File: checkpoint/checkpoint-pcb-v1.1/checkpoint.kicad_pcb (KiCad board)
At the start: 4 copper layers, 85.2 x 39.6 mm, 113 parts, among them J1 T0, J10 CAN_OUT, J11 BOOT, J12 Y_ENDSTOP, J13 I2C, J14 SERVO, J15 RGB, J16 SWD, J17 USB_C_Receptacle_USB2.0_16P, J18 PWR_OUT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

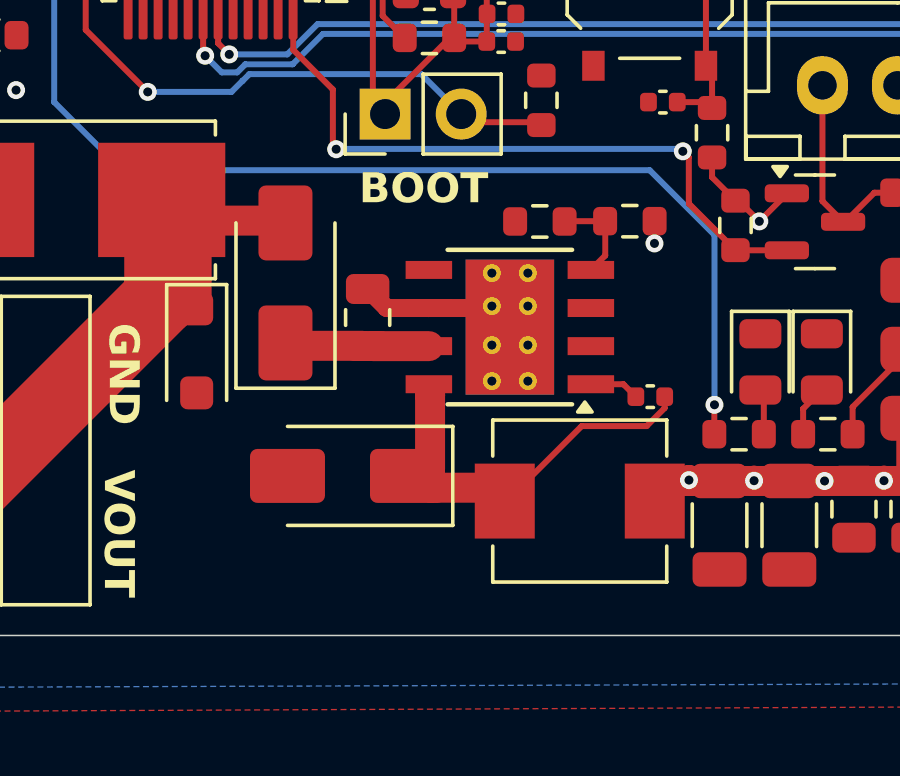
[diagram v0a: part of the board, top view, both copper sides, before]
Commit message: feat: add inductor to support 3A@5V output
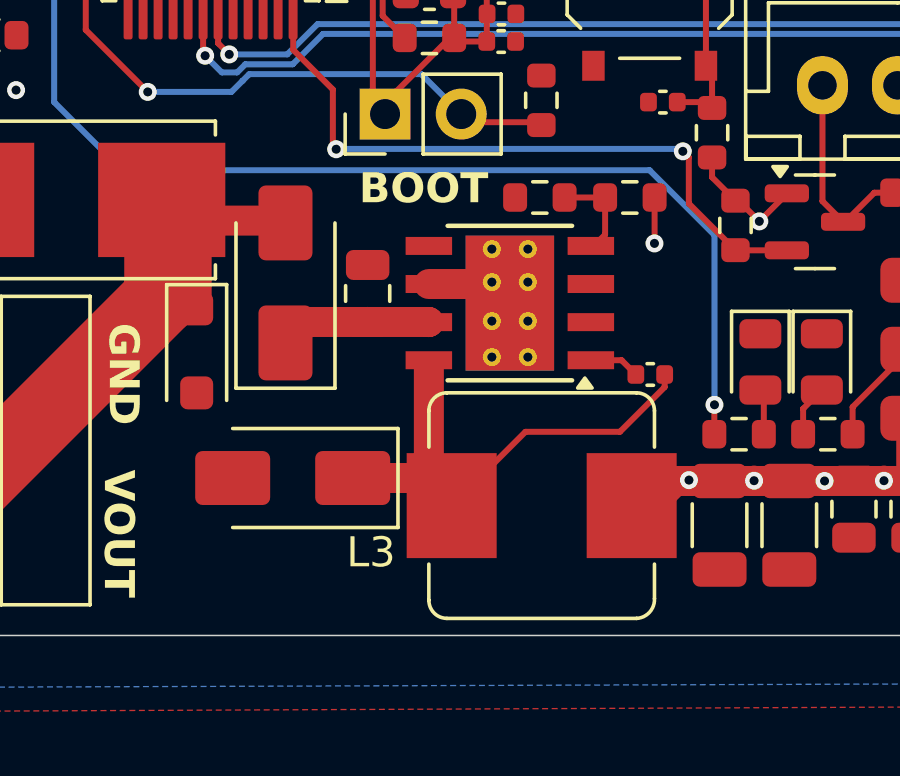
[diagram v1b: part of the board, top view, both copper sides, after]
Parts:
- L3: value 22uH -> 47uH; footprint Library:SMMS0530 -> Library:L_Bourns_SRP7050WA_7.9x7.3mm
- moved D11 1.83 mm to (65.2, 68.5)
- moved L3 1.28 mm to (73.5, 69.4)
- moved C27 0.80 mm to (67.7, 62.3)
- moved U6 0.80 mm to (72.5, 62.6)
- moved R36 0.80 mm to (73.5, 59.1)
- moved R35 0.79 mm to (76.5, 59.1)
- moved C28 0.74 mm to (77.1, 65.0)
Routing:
- net Net-(D11-K): track 11.9 -> 18.1 mm
- net GND: track 32.1 -> 29.4 mm
- net Net-(D10-K): track 4.19 -> 5.07 mm
- net +5V: track 16.2 -> 16.8 mm

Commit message: chore: update component rotation
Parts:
- C1, C10, C14, C18, C19, C2, C21, C22, C24, C26, C28, C3, C4, C5, C6, C7, C9: value 0.1uF -> 100nF
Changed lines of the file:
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@@
 		(sheetname "Thermistors")
 		(sheetfile "thermistors.kicad_sch")
-		(attr through_hole exclude_from_pos_files exclude_from_bom)
+		(attr through_hole exclude_from_pos_files)
 		(fp_line
 			(start -1.6 -2.75)
@@
 			)
 		)
-		(property "Value" "0.1uF"
+		(property "Value" "100nF"
 			(at 0 1.16 180)
 			(layer "F.Fab")
@@
 			)
 		)
-		(property "Value" "0.1uF"
+		(property "Value" "100nF"
 			(at 0 1.16 180)
 			(layer "F.Fab")
@@
 			)
 		)
-		(property "Value" "0.1uF"
+		(property "Value" "100nF"
 			(at 0.35 1.42 180)
 			(layer "F.Fab")
@@
 		(sheetname "CANBUS")
 		(sheetfile "canbus.kicad_sch")
-		(attr through_hole exclude_from_pos_files exclude_from_bom)
+		(attr through_hole exclude_from_pos_files)
 		(fp_line
 			(start -1.33 3.87)
@@
 			)
 		)
-		(property "Value" "0.1uF"
+		(property "Value" "100nF"
 			(at -0.75 0.1225 90)
 			(layer "F.Fab")
@@
 			)
 		)
-		(property "Value" "0.1uF"
+		(property "Value" "100nF"
 			(at 0 1.16 180)
 			(layer "F.Fab")
@@
 			)
 		)
-		(property "Value" "0.1uF"
+		(property "Value" "100nF"
 			(at 1.905589 1.16 90)
 			(layer "F.Fab")
@@
 			)
 		)
-		(property "Value" "0.1uF"
+		(property "Value" "100nF"
 			(at 0.0025 1.14 0)
 			(layer "F.Fab")
@@
 		(sheetname "Thermistors")
 		(sheetfile "thermistors.kicad_sch")
-		(attr through_hole exclude_from_pos_files exclude_from_bom)
+		(attr through_hole exclude_from_pos_files)
 		(fp_line
 			(start -1.6 -2.75)
@@
 		(sheetname "CANBUS")
 		(sheetfile "canbus.kicad_sch")
-		(attr through_hole exclude_from_pos_files exclude_from_bom)
+		(attr through_hole exclude_from_pos_files)
 		(fp_line
 			(start -2.56 3.51)
@@
 		(sheetname "Power")
 		(sheetfile "power.kicad_sch")
-		(attr through_hole exclude_from_pos_files exclude_from_bom)
+		(attr through_hole exclude_from_pos_files)
 		(fp_line
 			(start -2.84 4.9)
@@
 			)
 		)
-		(property "Value" "0.1uF"
+		(property "Value" "100nF"
 			(at 0.05 -1.05 180)
 			(layer "F.Fab")
@@
 		(sheetname "USB")
 		(sheetfile "usb.kicad_sch")
-		(attr through_hole exclude_from_pos_files exclude_from_bom)
+		(attr through_hole exclude_from_pos_files)
 		(fp_line
 			(start -1.33 3.87)
@@
 		(sheetname "Thermistors")
 		(sheetfile "thermistors.kicad_sch")
-		(attr through_hole exclude_from_pos_files exclude_from_bom)
+		(attr through_hole exclude_from_pos_files)
 		(fp_line
 			(start 1.33 1.27)
@@
 			)
 		)
-		(property "Value" "0.1uF"
+		(property "Value" "100nF"
 			(at -0.005 -0.98 0)
 			(layer "F.Fab")
@@
 		(sheetname "MCU")
 		(sheetfile "mcu.kicad_sch")
-		(attr through_hole exclude_from_pos_files exclude_from_bom)
+		(attr through_hole exclude_from_pos_files)
 		(fp_line
 			(start 7.56 3.51)
@@
 			)
 		)
-		(property "Value" "0.1uF"
+		(property "Value" "100nF"
 			(at 0.085 -1.05 90)
 			(layer "F.Fab")
@@
 			)
 		)
-		(property "Value" "0.1uF"
+		(property "Value" "100nF"
 			(at 0 1.16 0)
 			(layer "F.Fab")
@@
 		(sheetname "MCU")
 		(sheetfile "mcu.kicad_sch")
-		(attr through_hole exclude_from_pos_files exclude_from_bom)
+		(attr through_hole exclude_from_pos_files)
 		(fp_line
 			(start -1.33 -1.33)
@@
 		(sheetname "Thermistors")
 		(sheetfile "thermistors.kicad_sch")
-		(attr through_hole exclude_from_pos_files exclude_from_bom)
+		(attr through_hole exclude_from_pos_files)
 		(fp_line
 			(start -1.33 -1.33)
@@
 			)
 		)
-		(property "Value" "0.1uF"
+		(property "Value" "100nF"
 			(at 0 1.16 0)
 			(layer "F.Fab")
@@
 		(sheetname "Thermistors")
 		(sheetfile "thermistors.kicad_sch")
-		(attr through_hole exclude_from_pos_files exclude_from_bom)
+		(attr through_hole exclude_from_pos_files)
 		(fp_line
 			(start -1.6 -2.75)
@@
 		(sheetname "Thermistors")
 		(sheetfile "thermistors.kicad_sch")
-		(attr through_hole exclude_from_pos_files exclude_from_bom)
+		(attr through_hole exclude_from_pos_files)
 		(fp_line
 			(start -1.33 -1.33)
@@
 		(sheetname "Power")
 		(sheetfile "power.kicad_sch")
-		(attr smd exclude_from_pos_files exclude_from_bom)
+		(attr smd exclude_from_pos_files)
 		(fp_line
 			(start -3.76 -1.95)
@@
 			)
 		)
-		(property "Value" "0.1uF"
+		(property "Value" "100nF"
 			(at 0 0 0)
 			(layer "F.Fab")
@@
 		(sheetname "MCU")
 		(sheetfile "mcu.kicad_sch")
-		(attr through_hole exclude_from_pos_files exclude_from_bom)
+		(attr through_hole exclude_from_pos_files)
 		(fp_line
 			(start -1.33 -1.33)
@@
 			)
 		)
-		(property "Value" "0.1uF"
+		(property "Value" "100nF"
 			(at 0 1.025 90)
 			(layer "F.Fab")
@@
 			)
 		)
-		(property "Value" "0.1uF"
+		(property "Value" "100nF"
 			(at 0 1.14 0)
 			(layer "F.Fab")
@@
 		(sheetname "MCU")
 		(sheetfile "mcu.kicad_sch")
-		(attr through_hole exclude_from_pos_files exclude_from_bom)
+		(attr through_hole exclude_from_pos_files)
 		(fp_line
 			(start 7.56 3.51)
@@
 		(sheetname "Thermistors")
 		(sheetfile "thermistors.kicad_sch")
-		(attr through_hole exclude_from_pos_files exclude_from_bom)
+		(attr through_hole exclude_from_pos_files)
 		(fp_line
 			(start -1.6 -2.75)
@@
 			)
 		)
-		(property "Value" "0.1uF"
+		(property "Value" "100nF"
 			(at 0 1.16 90)
 			(layer "F.Fab")
@@
 		(sheetname "MCU")
 		(sheetfile "mcu.kicad_sch")
-		(attr through_hole exclude_from_pos_files exclude_from_bom)
+		(attr through_hole exclude_from_pos_files)
 		(fp_line
 			(start -1.6 -2.75)
@@
 			)
 		)
-		(property "Value" "0.1uF"
+		(property "Value" "100nF"
 			(at 0 1.16 180)
 			(layer "F.Fab")
@@
 		(sheetname "Thermistors")
 		(sheetfile "thermistors.kicad_sch")
-		(attr through_hole exclude_from_pos_files exclude_from_bom)
+		(attr through_hole exclude_from_pos_files)
 		(fp_line
 			(start 1.33 1.27)
@@
 		(sheetname "Thermistors")
 		(sheetfile "thermistors.kicad_sch")
-		(attr through_hole exclude_from_pos_files exclude_from_bom)
+		(attr through_hole exclude_from_pos_files)
 		(fp_line
 			(start -1.6 -2.75)
@@
 		(sheetname "Power")
 		(sheetfile "power.kicad_sch")
-		(attr through_hole exclude_from_pos_files exclude_from_bom)
+		(attr through_hole exclude_from_pos_files)
 		(fp_line
 			(start 6.685 2.58)
@@
 		(sheetname "MCU")
 		(sheetfile "mcu.kicad_sch")
-		(attr through_hole exclude_from_pos_files exclude_from_bom)
+		(attr through_hole exclude_from_pos_files)
 		(fp_line
 			(start -2.559999 -9.31)
